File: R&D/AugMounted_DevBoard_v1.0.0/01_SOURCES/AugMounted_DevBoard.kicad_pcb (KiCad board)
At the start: 2 copper layers, 0 parts

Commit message: Schematic 90% done
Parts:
- added C1: C_0603_100nF_100V_X7R_10%, .mounted-lib:C_0603_1608Metric, F.Cu at (79.2, 96.4)
- added C10: C_0603_100nF_100V_X7R_10%, .mounted-lib:C_0603_1608Metric, F.Cu at (83.5, 96.4)
- added C11: C_0805_1uF_100V_X7S_20%, .mounted-lib:C_0805_1608Metric, F.Cu at (74.9, 108.8)
- added C12: C_0603_100nF_100V_X7R_10%, .mounted-lib:C_0603_1608Metric, F.Cu at (83.5, 99.1)
- added C13: C_0603_100nF_100V_X7R_10%, .mounted-lib:C_0603_1608Metric, F.Cu at (83.5, 101.7)
- added C14: C_0603_100nF_100V_X7R_10%, .mounted-lib:C_0603_1608Metric, F.Cu at (83.5, 104.4)
- added C15: C_0603_100nF_100V_X7R_10%, .mounted-lib:C_0603_1608Metric, F.Cu at (83.5, 107.0)
- added C16: C_0603_100nF_100V_X7R_10%, .mounted-lib:C_0603_1608Metric, F.Cu at (87.7, 96.4)
- added C17: C_0603_100nF_100V_X7R_10%, .mounted-lib:C_0603_1608Metric, F.Cu at (87.7, 99.1)
- added C18: C_0805_1uF_100V_X7S_20%, .mounted-lib:C_0805_1608Metric, F.Cu at (78.9, 57.0)
- added C19: C_0805_1uF_100V_X7S_20%, .mounted-lib:C_0805_1608Metric, F.Cu at (78.9, 60.0)
- added C2: C_0805_1uF_100V_X7S_20%, .mounted-lib:C_0805_1608Metric, F.Cu at (74.9, 96.6)
- added C20: C_0805_2.2uF_25V_X7R_20%, .mounted-lib:C_0805_1608Metric, F.Cu at (78.9, 63.1)
- added C21: C_0603_100nF_100V_X7R_10%, .mounted-lib:C_0603_1608Metric, F.Cu at (66.0, 56.8)
- added C22: C_0603_1.2nF_100V_X7R_5%, .mounted-lib:C_0603_1608Metric, F.Cu at (66.0, 59.4)
- added C23: C_1206_10uF_25V_X7R_10%, .mounted-lib:C_1206_3216Metric, F.Cu at (88.4, 57.1)
- added C24: C_1206_10uF_25V_X7R_10%, .mounted-lib:C_1206_3216Metric, F.Cu at (88.4, 60.5)
- added C25: C_1206_10uF_25V_X7R_10%, .mounted-lib:C_1206_3216Metric, F.Cu at (88.4, 63.8)
- added C26: C_1206_10uF_25V_X7R_10%, .mounted-lib:C_1206_3216Metric, F.Cu at (88.4, 67.2)
- added C27: C_0805_2.2uF_25V_X7R_20%, .mounted-lib:C_0805_1608Metric, F.Cu at (78.9, 66.1)
- added C28: C_0805_10uF_10V_X7R_10%, .mounted-lib:C_0805_1608Metric, F.Cu at (78.9, 69.2)
- added C29: C_0603_100nF_100V_X7R_10%, .mounted-lib:C_0603_1608Metric, F.Cu at (113.5, 116.7)
- added C3: C_0603_100nF_100V_X7R_10%, .mounted-lib:C_0603_1608Metric, F.Cu at (79.2, 99.1)
- added C30: C_0603_2.2uF_10V_X7R_10%, .mounted-lib:C_0603_1608Metric, F.Cu at (113.5, 119.4)
- added C31: C_0603_100nF_100V_X7R_10%, .mounted-lib:C_0603_1608Metric, F.Cu at (66.0, 62.1)
- added C32: C_0805_10uF_10V_X7R_10%, .mounted-lib:C_0805_1608Metric, F.Cu at (78.9, 72.2)
- added C33: C_0805_10uF_10V_X7R_10%, .mounted-lib:C_0805_1608Metric, F.Cu at (83.3, 57.0)
- added C36: C_0805_10uF_10V_X7R_10%, .mounted-lib:C_0805_1608Metric, F.Cu at (83.3, 60.0)
- added C37: C_0805_10uF_10V_X7R_10%, .mounted-lib:C_0805_1608Metric, F.Cu at (83.3, 63.1)
- added C38: C_0603_47nF_100V_X7R_10%, .mounted-lib:C_0603_1608Metric, F.Cu at (66.0, 64.7)
- added C39: C_0603_4.7uF_16V_X7R_10%, .mounted-lib:C_0603_1608Metric, F.Cu at (66.0, 67.4)
- added C4: C_0805_1uF_100V_X7S_20%, .mounted-lib:C_0805_1608Metric, F.Cu at (74.9, 99.7)
- added C40: C_0805_10uF_10V_X7R_10%, .mounted-lib:C_0805_1608Metric, F.Cu at (83.3, 66.1)
- added C41: C_0805_10uF_10V_X7R_10%, .mounted-lib:C_0805_1608Metric, F.Cu at (83.3, 69.2)
- added C42: C_0603_1uF_16V_X7R_10%, .mounted-lib:C_0603_1608Metric, F.Cu at (66.0, 70.0)
- added C43: C_0603_100nF_100V_X7R_10%, .mounted-lib:C_0603_1608Metric, F.Cu at (66.0, 72.7)
- added C5: C_0805_1uF_100V_X7S_20%, .mounted-lib:C_0805_1608Metric, F.Cu at (74.9, 102.7)
- added C6: C_0805_1uF_100V_X7S_20%, .mounted-lib:C_0805_1608Metric, F.Cu at (74.9, 105.8)
- added C7: C_0603_100nF_100V_X7R_10%, .mounted-lib:C_0603_1608Metric, F.Cu at (79.2, 101.7)
- added C8: C_0603_100nF_100V_X7R_10%, .mounted-lib:C_0603_1608Metric, F.Cu at (79.2, 104.4)
- added C9: C_0603_100nF_100V_X7R_10%, .mounted-lib:C_0603_1608Metric, F.Cu at (79.2, 107.0)
- added D1: D_V2FM10HM3/H, .mounted-lib:D_SMF_VISHAY, F.Cu at (109.2, 113.7)
- added D2: D_V2FM10HM3/H, .mounted-lib:D_SMF_VISHAY, F.Cu at (94.2, 63.5)
- added D3: D_SRV05-4, .mounted-lib:SOT-23-6_TECH_PUBLIC, F.Cu at (108.8, 117.6)
- added D4: D_1SS301, .mounted-lib:SOT-23_TOSHIBA, F.Cu at (88.5, 86.3)
- added D5: D_SRV05-4, .mounted-lib:SOT-23-6_TECH_PUBLIC, F.Cu at (93.8, 71.0)
- added J1: J_TYPE-C-31-M-13, .mounted-lib:J_TYPE-C-31-M-13, F.Cu at (99.0, 120.6)
- added J2: J_FH43BW-61S-0.2SHW, .mounted-lib:J_FH43BW-61S-0.2SHW, F.Cu at (80.4, 92.8)
- added J3: J_JST_S2B-PH-SM4-TB, .mounted-lib:J_JST_S2B-PH-SM4-TB, F.Cu at (81.5, 79.4)
- added JP1: SolderJumper_2_Bridged, Jumper:SolderJumper-2_P1.3mm_Bridged_RoundedPad1.0x1.5mm, F.Cu at (79.3, 110.1)
- added JP2: SolderJumper_2_Bridged, Jumper:SolderJumper-2_P1.3mm_Bridged_RoundedPad1.0x1.5mm, F.Cu at (79.3, 113.7)
- added JP3: SolderJumper_2_Bridged, Jumper:SolderJumper-2_P1.3mm_Bridged_RoundedPad1.0x1.5mm, F.Cu at (79.3, 117.2)
- added L1: L_7447789003, .mounted-lib:L_7447789003, F.Cu at (68.4, 81.5)
- added L3: L_TFM252012ALMA1R0MTAA, .mounted-lib:TFM252012ALMA1R0MTAA, F.Cu at (79.1, 86.4)
- added L4: L_FNR3015S2R2MT, .mounted-lib:L_FNR3015S2R2MT, F.Cu at (111.8, 87.8)
- added Q1: Q_BSS123WQ-7-F, .mounted-lib:SOT-323_SC-70_DIODES_INC, F.Cu at (86.3, 110.3)
- added Q2: Q_BSS123WQ-7-F, .mounted-lib:SOT-323_SC-70_DIODES_INC, F.Cu at (94.0, 75.7)
- added Q3: Q_HSS2P10, .mounted-lib:SOT-23-3_HUASHUO, F.Cu at (87.8, 71.1)
- added Q5: Q_BSS123WQ-7-F, .mounted-lib:SOT-323_SC-70_DIODES_INC, F.Cu at (94.0, 79.5)
- added R1: R_0603_100k_1%_0.1W, .mounted-lib:R_0603_1608Metric, F.Cu at (87.7, 101.7)
- added R10: R_0603_100k_1%_0.1W, .mounted-lib:R_0603_1608Metric, F.Cu at (70.3, 70.0)
- added R11: R_0603_0R_1%_0.1W, .mounted-lib:R_0603_1608Metric, F.Cu at (70.3, 72.7)
- added R13: R_0603_1M_1%_0.1W, .mounted-lib:R_0603_1608Metric, F.Cu at (70.3, 75.3)
- added R14: R_0603_10k_1%_0.1W, .mounted-lib:R_0603_1608Metric, F.Cu at (74.5, 56.8)
- added R15: R_0603_31.2k_0.5%_0.1W, .mounted-lib:R_0603_1608Metric, F.Cu at (74.5, 59.4)
- added R16: R_0603_5.23k_1%_0.1W, .mounted-lib:R_0603_1608Metric, F.Cu at (74.5, 62.1)
- added R17: R_0603_10k_1%_0.1W, .mounted-lib:R_0603_1608Metric, F.Cu at (74.5, 64.7)
- added R18: R_0603_10k_1%_0.1W, .mounted-lib:R_0603_1608Metric, F.Cu at (74.5, 67.4)
- added R19: R_0603_316R_0.5%_0.1W, .mounted-lib:R_0603_1608Metric, F.Cu at (74.5, 70.0)
- added R2: R_0603_100k_1%_0.1W, .mounted-lib:R_0603_1608Metric, F.Cu at (87.7, 104.4)
- added R21: R_0603_100k_1%_0.1W, .mounted-lib:R_0603_1608Metric, F.Cu at (74.5, 72.7)
- added R3: R_0603_100k_1%_0.1W, .mounted-lib:R_0603_1608Metric, F.Cu at (66.0, 75.3)
- added R4: R_0603_42.2k_1%_0.1W, .mounted-lib:R_0603_1608Metric, F.Cu at (70.3, 56.8)
- added R5: R_0603_200k_1%_0.1W, .mounted-lib:R_0603_1608Metric, F.Cu at (70.3, 59.4)
- added R6: R_0603_26.7k_1%_0.1W, .mounted-lib:R_0603_1608Metric, F.Cu at (70.3, 62.1)
- added R7: R_0603_100k_1%_0.1W, .mounted-lib:R_0603_1608Metric, F.Cu at (70.3, 64.7)
- added R9: R_0603_100k_1%_0.1W, .mounted-lib:R_0603_1608Metric, F.Cu at (70.3, 67.4)
- added RT1: RT_TX06F103F3435ER, .mounted-lib:NTCG16_XXX_TDK, F.Cu at (93.8, 87.1)
- added SJ1: SOLDER_JUMPER_3PIN_NC, .mounted-lib:SOLDER_JUMPER_3PIN_NC, F.Cu at (94.0, 67.0)
- added TP1: TESTPOINT_1MM, .mounted-lib:TESTPOINT_1MM, F.Cu at (82.8, 109.7)
- added TP2: TESTPOINT_1MM, .mounted-lib:TESTPOINT_1MM, F.Cu at (82.8, 112.3)
- added TP3: TESTPOINT_1MM, .mounted-lib:TESTPOINT_1MM, F.Cu at (82.8, 115.0)
- added TP4: TESTPOINT_1.5MM, .mounted-lib:TESTPOINT_1.5MM, F.Cu at (74.5, 78.2)
- added U1: ESP32-S3-WROOM-1U-N16R8, .mounted-lib:ESP32-S3-WROOM-1U, F.Cu at (102.2, 100.8)
- added U10: U_TPS63001DRCR, .mounted-lib:PVSON-N10_TEXAS_INSTRUMENTS, F.Cu at (89.1, 81.8)
- added U2: U_BQ24296MRGER, .mounted-lib:VQFN-24_TEXAS_INSTRUMENTS, F.Cu at (94.3, 58.6)
- added U3: U_MAX17048G+T10, .mounted-lib:TDFN-8_MAXIM_INTEGRATED, F.Cu at (83.8, 86.3)
- added U4: U_TXB0108PWR, .mounted-lib:TSSOP-20_4.4x6.5mm_P0.65mm_TEXAS_INSTRUMENTS, F.Cu at (68.3, 94.4)
- added U5: U_TXB0108PWR, .mounted-lib:TSSOP-20_4.4x6.5mm_P0.65mm_TEXAS_INSTRUMENTS, F.Cu at (68.3, 102.4)
- added U6: U_TXB0108PWR, .mounted-lib:TSSOP-20_4.4x6.5mm_P0.65mm_TEXAS_INSTRUMENTS, F.Cu at (68.3, 110.5)
- added U7: U_TPS61087DRCR, .mounted-lib:PVSON-N10_TEXAS_INSTRUMENTS, F.Cu at (89.1, 76.4)
- added U8: U_LP3987H-18B5F, .mounted-lib:SOT-23-5_LOW_POWER, F.Cu at (94.3, 83.7)
- added U9: U_VCNL4040M3OE, .mounted-lib:VCNL4040_4X2X1.1_VISHAY, F.Cu at (114.6, 93.4)
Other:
- board outline added: 9.5 x 6.5 mm

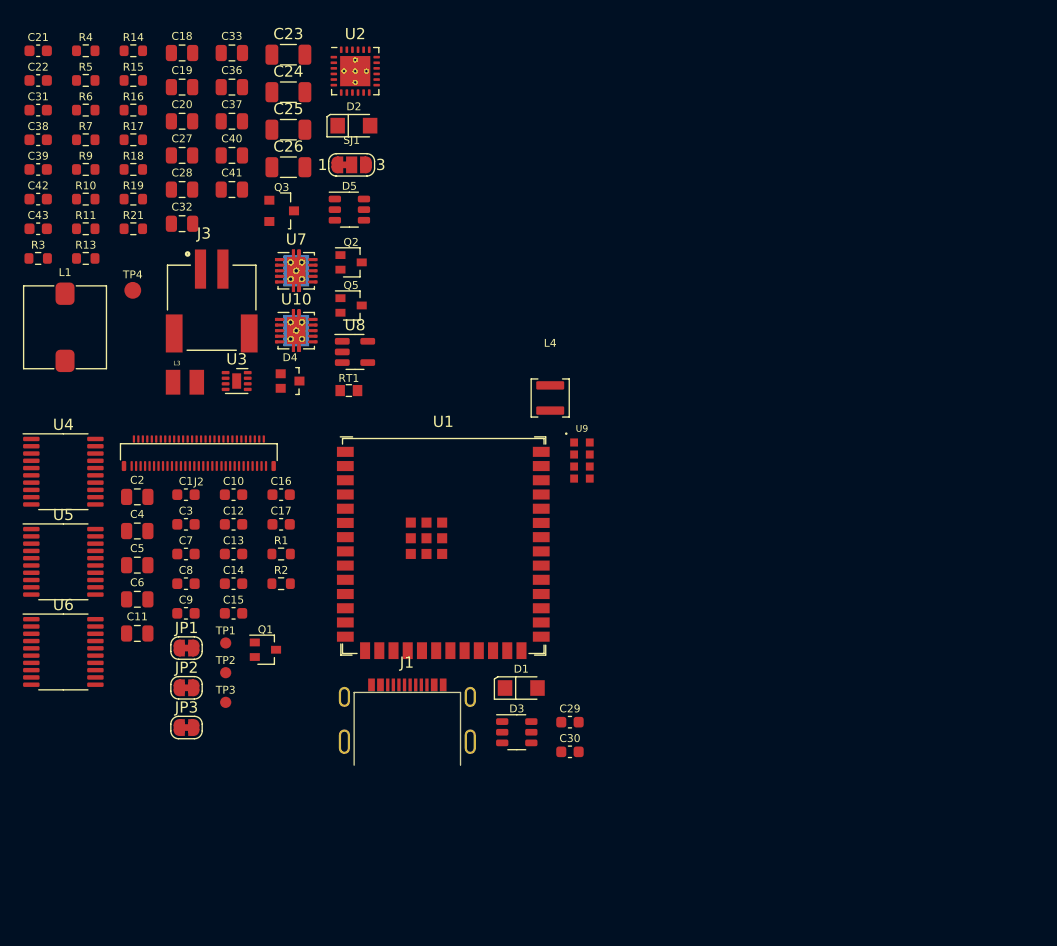
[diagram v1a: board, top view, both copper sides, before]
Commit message: Schematic done
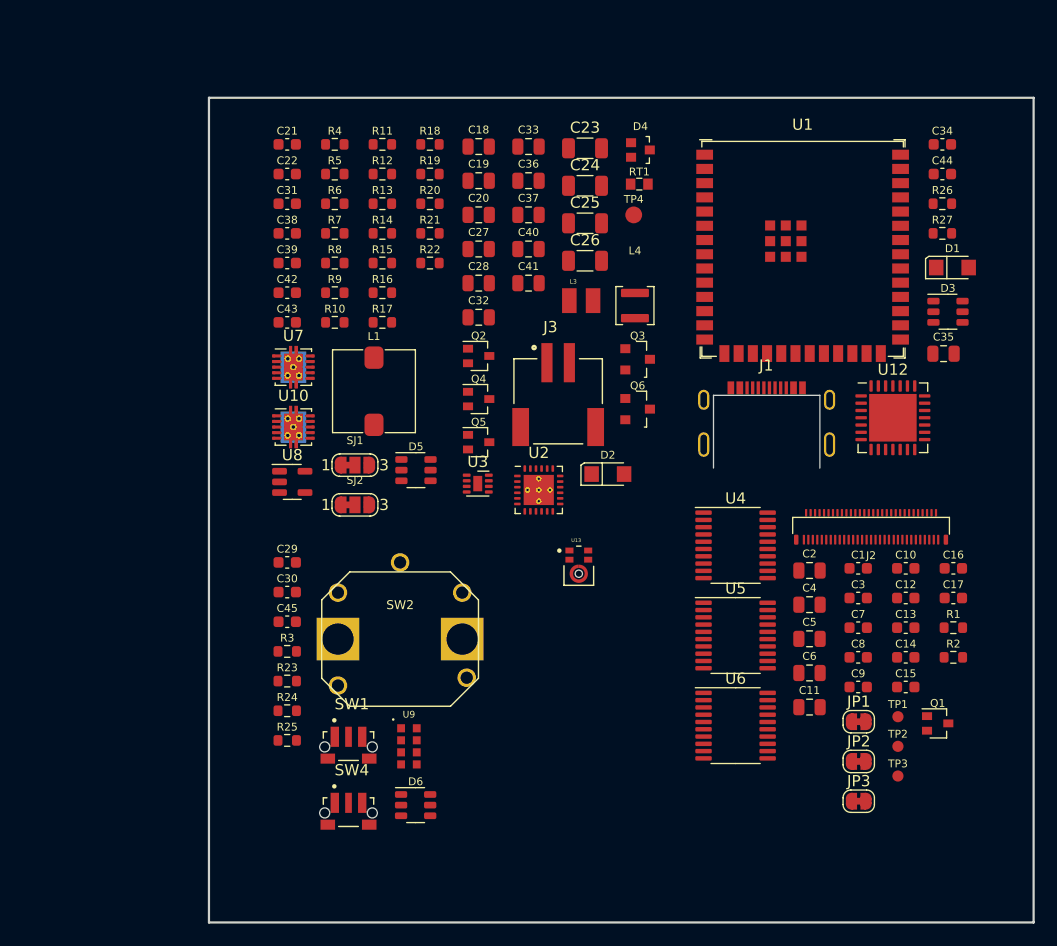
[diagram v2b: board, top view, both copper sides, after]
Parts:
- added C34: C_0603_100nF_100V_X7R_10%, .mounted-lib:C_0603_1608Metric, F.Cu at (146.8, 65.1)
- added C35: C_0805_22uF_10V_XR7_20%, .mounted-lib:C_0805_1608Metric, F.Cu at (146.9, 83.8)
- added C44: C_0603_100nF_100V_X7R_10%, .mounted-lib:C_0603_1608Metric, F.Cu at (146.8, 67.8)
- added C45: C_0603_100nF_100V_X7R_10%, .mounted-lib:C_0603_1608Metric, F.Cu at (88.3, 107.8)
- added D6: D_SRV05-4, .mounted-lib:SOT-23-6_TECH_PUBLIC, F.Cu at (99.7, 124.1)
- added Q4: Q_BSS123WQ-7-F, .mounted-lib:SOT-323_SC-70_DIODES_INC, F.Cu at (105.4, 87.9)
- added Q6: Q_HSS2P10, .mounted-lib:SOT-23-3_HUASHUO, F.Cu at (119.6, 88.8)
- added R12: R_0603_0R_1%_0.1W, .mounted-lib:R_0603_1608Metric, F.Cu at (96.8, 67.8)
- added R20: R_0603_100k_1%_0.1W, .mounted-lib:R_0603_1608Metric, F.Cu at (101.0, 70.4)
- added R22: R_0603_0R_1%_0.1W, .mounted-lib:R_0603_1608Metric, F.Cu at (101.0, 75.7)
- added R23: R_0603_10k_1%_0.1W, .mounted-lib:R_0603_1608Metric, F.Cu at (88.3, 113.1)
- added R24: R_0603_100k_1%_0.1W, .mounted-lib:R_0603_1608Metric, F.Cu at (88.3, 115.7)
- added R25: R_0603_100k_1%_0.1W, .mounted-lib:R_0603_1608Metric, F.Cu at (88.3, 118.4)
- added R26: R_0603_4.7k_1%_0.1W, .mounted-lib:R_0603_1608Metric, F.Cu at (146.8, 70.4)
- added R27: R_0603_4.7k_1%_0.1W, .mounted-lib:R_0603_1608Metric, F.Cu at (146.8, 73.1)
- added R8: R_0603_1M_1%_0.1W, .mounted-lib:R_0603_1608Metric, F.Cu at (92.5, 75.7)
- added SJ2: SOLDER_JUMPER_3PIN_NC, .mounted-lib:SOLDER_JUMPER_3PIN_NC, F.Cu at (94.3, 97.3)
- added SW1: SW_SKRTLAE010, .mounted-lib:SW_SKRTLAE010, F.Cu at (93.7, 118.9)
- added SW2: SW_EC12D1564404, .mounted-lib:SW_EC12D1564404, F.Cu at (98.4, 109.3)
- added SW4: SW_SKRTLAE010, .mounted-lib:SW_SKRTLAE010, F.Cu at (93.7, 124.8)
- added U12: U_MCP23017T-E/ML, .mounted-lib:QFN-28-1EP_6x6mm_P0.65mm_EP4.25x4.25mm_MICROCHIP, F.Cu at (142.4, 89.5)
- added U13: ICS‐41350, .mounted-lib:U_ICS-41350, F.Cu at (114.3, 102.8)
- C29: value C_0603_100nF_100V_X7R_10% -> C_0603_2.2uF_10V_X7R_10%
- C30: value C_0603_2.2uF_10V_X7R_10% -> C_0603_100nF_100V_X7R_10%
- R11: value R_0603_0R_1%_0.1W -> R_0603_1M_1%_0.1W
- R3: value R_0603_100k_1%_0.1W -> R_0603_10k_1%_0.1W
- moved C1 60.4 mm to (139.3, 103.0)
- moved C10 60.4 mm to (143.5, 103.0)
- moved C12 60.4 mm to (143.5, 105.6)
- moved C13 60.4 mm to (143.5, 108.3)
- moved C14 60.4 mm to (143.5, 110.9)
- moved C15 60.4 mm to (143.5, 113.6)
- moved C16 60.4 mm to (147.8, 103.0)
- moved C17 60.4 mm to (147.8, 105.6)
- moved C3 60.4 mm to (139.3, 105.6)
- moved C7 60.4 mm to (139.3, 108.3)
- moved C8 60.4 mm to (139.3, 110.9)
- moved C9 60.4 mm to (139.3, 113.6)
- moved R1 60.4 mm to (147.8, 108.3)
- moved R2 60.4 mm to (147.8, 110.9)
- moved Q1 60.4 mm to (146.4, 116.8)
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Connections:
- net /Battery Management/BUTTON_PIN renamed /Battery Management/ENCODER_BUTTON
- net /OLED/VDD1 renamed /1.8V_LCD
- net Net-(D4-A1) renamed /ENCODER_S2
- net Net-(U2-STAT) renamed /Battery Management/CHARGE_STATUS
- net Net-(U2-~{PG}) renamed /Battery Management/PGOOD
- C42 pad 1: Net-(C42-Pad1) -> VBUS
- D1 pad 1: unconnected-(D1-K-Pad1) -> VBUS
- D1 pad 2: unconnected-(D1-A-Pad2) -> /MCU/VBUS_USB
- D3 pad 1: unconnected-(D3-IO1-Pad1) -> /MCU/USB_D+
- D3 pad 2: unconnected-(D3-VN-Pad2) -> GND
- D3 pad 3: unconnected-(D3-IO2-Pad3) -> /MCU/CC1
- D3 pad 4: unconnected-(D3-IO3-Pad4) -> /MCU/USB_D-
- D3 pad 5: unconnected-(D3-VP-Pad5) -> /MCU/VBUS_USB
- D3 pad 6: unconnected-(D3-IO4-Pad6) -> /MCU/CC2
- J1 pad A1: Net-(J1-GND-PadA1) -> GND
- J1 pad A12: Net-(J1-GND-PadA1) -> GND
- J1 pad A4: Net-(J1-VBUS-PadA4) -> /MCU/VBUS_USB
- J1 pad A6: unconnected-(J1-DP1-PadA6) -> /MCU/USB_D+
- J1 pad A7: unconnected-(J1-DN1-PadA7) -> /MCU/USB_D-
- J1 pad A9: Net-(J1-VBUS-PadA4) -> /MCU/VBUS_USB
- J1 pad B1: Net-(J1-GND-PadA1) -> GND
- J1 pad B12: Net-(J1-GND-PadA1) -> GND
- J1 pad B4: Net-(J1-VBUS-PadA4) -> /MCU/VBUS_USB
- J1 pad B6: unconnected-(J1-DP2-PadB6) -> /MCU/USB_D+
- J1 pad B7: unconnected-(J1-DN2-PadB7) -> /MCU/USB_D-
- J1 pad B9: Net-(J1-VBUS-PadA4) -> /MCU/VBUS_USB
- J1 pad GND: Net-(J1-GND-PadA1) -> GND
- J2 pad 26: /OLED/G2_1.8V -> /OLED/RGB_LSB_1.8V
- R11 pad 1: Net-(Q3-G) -> /Battery Management/1.8V_ENABLE
- R11 pad 2: Net-(Q2-D) -> GND
- R3 pad 1: /Battery Management/1.8V_ENABLE -> +3.3V
- R3 pad 2: GND -> /ENCODER_B
- R9 pad 2: Net-(R9-Pad2) -> /ENCODER_S1
- U1 pad 1: Net-(U1-GND-Pad1) -> GND
- U1 pad 10: unconnected-(U1-GPIO17/U1TXD/ADC2_CH6-Pad10) -> /ENCODER_B
- U1 pad 11: unconnected-(U1-GPIO18/U1RXD/ADC2_CH7/CLK_OUT3-Pad11) -> /ENCODER_A
- U1 pad 12: unconnected-(U1-GPIO8/TOUCH8/ADC1_CH7/SUBSPICS1-Pad12) -> /XCLR
- U1 pad 13: unconnected-(U1-GPIO19/U1RTS/ADC2_CH8/CLK_OUT2/USB_D--Pad13) -> /MCU/USB_D-
- U1 pad 14: unconnected-(U1-GPIO20/U1CTS/ADC2_CH9/CLK_OUT1/USB_D+-Pad14) -> /MCU/USB_D+
- U1 pad 15: unconnected-(U1-GPIO3/TOUCH3/ADC1_CH2-Pad15) -> /XHD
- U1 pad 16: unconnected-(U1-GPIO46-Pad16) -> /HVD
- U1 pad 17: unconnected-(U1-GPIO9/TOUCH9/ADC1_CH8/FSPIHD/SUBSPIHD-Pad17) -> /MCLK
- U1 pad 18: unconnected-(U1-GPIO10/TOUCH10/ADC1_CH9/FSPICS0/FSPIIO4/SUBSPICS0-Pad18) -> /B5
- U1 pad 19: unconnected-(U1-GPIO11/TOUCH11/ADC2_CH0/FSPID/FSPIIO5/SUBSPID-Pad19) -> /B4
- U1 pad 2: unconnected-(U1-3V3-Pad2) -> +3.3V
- U1 pad 20: unconnected-(U1-GPIO12/TOUCH12/ADC2_CH1/FSPICLK/FSPIIO6/SUBSPICLK-Pad20) -> /B3
- U1 pad 21: unconnected-(U1-GPIO13/TOUCH13/ADC2_CH2/FSPIQ/FSPIIO7/SUBSPIQ-Pad21) -> /B2
- U1 pad 22: unconnected-(U1-GPIO14/TOUCH14/ADC2_CH3/FSPIWP/FSPIDQS/SUBSPIWP-Pad22) -> /B1
- U1 pad 23: unconnected-(U1-GPIO21-Pad23) -> /I2S_PDM_DATA
- U1 pad 24: unconnected-(U1-GPIO47/SPICLK_P/SUBSPICLK_P_DIFF-Pad24) -> /G5
- U1 pad 25: unconnected-(U1-GPIO48/SPICLK_N/SUBSPICLK_N_DIFF-Pad25) -> /G4
- U1 pad 26: unconnected-(U1-GPIO45-Pad26) -> /G3
- U1 pad 31: unconnected-(U1-GPIO38/FSPIWP/SUBSPIWP-Pad31) -> /G2
- U1 pad 32: unconnected-(U1-MTCK/GPIO39/CLK_OUT3/SUBSPICS1-Pad32) -> /G1
- U1 pad 33: unconnected-(U1-MTDO/GPIO40/CLK_OUT2-Pad33) -> /R5
- U1 pad 34: unconnected-(U1-MTDI/GPIO41/CLK_OUT1-Pad34) -> /R4
- U1 pad 35: unconnected-(U1-MTMS/GPIO42-Pad35) -> /R3
- U1 pad 36: unconnected-(U1-U0RXD/GPIO44/CLK_OUT2-Pad36) -> /Battery Management/ESP_POWER_EN
- U1 pad 37: unconnected-(U1-U0TXD/GPIO43/CLK_OUT1-Pad37) -> /R2
- U1 pad 38: unconnected-(U1-GPIO2/TOUCH2/ADC1_CH1-Pad38) -> /SCL
- U1 pad 39: unconnected-(U1-GPIO1/TOUCH1/ADC1_CH0-Pad39) -> /R1
- U1 pad 4: unconnected-(U1-GPIO4/TOUCH4/ADC1_CH3-Pad4) -> /MISO
- U1 pad 40: Net-(U1-GND-Pad1) -> GND
- U1 pad 41: Net-(U1-GND-Pad1) -> GND
- U1 pad 5: unconnected-(U1-GPIO5/TOUCH5/ADC1_CH4-Pad5) -> /MOSI
- U1 pad 6: unconnected-(U1-GPIO6/TOUCH6/ADC1_CH5-Pad6) -> /SCK
- U1 pad 7: unconnected-(U1-GPIO7/TOUCH7/ADC1_CH6-Pad7) -> /CS
- U1 pad 8: unconnected-(U1-GPIO15/U0RTS/ADC2_CH4/XTAL_32K_P-Pad8) -> /SDA
- U1 pad 9: unconnected-(U1-GPIO16/U0CTS/ADC2_CH5/XTAL_32K_N-Pad9) -> /I2S_PDM_CLK
- U2 pad 1: Net-(C42-Pad1) -> VBUS
- U2 pad 2: GND -> Net-(SJ2-C)
- U2 pad 24: Net-(C42-Pad1) -> VBUS
- U2 pad 25: unconnected-(U2-PAD-Pad25) -> GND
- U2 pad 5: /Battery Management/SCL -> /SCL
- U2 pad 6: /Battery Management/SDA -> /SDA
- U3 pad 7: /Battery Management/SCL -> /SCL
- U3 pad 8: /Battery Management/SDA -> /SDA
- U4 pad 12: /OLED/G3 -> /G2
- U4 pad 13: /OLED/G2 -> /G1
- U4 pad 14: /OLED/G1 -> unconnected-(U4-B6-Pad14)
- U4 pad 15: /OLED/R5 -> /R5
- U4 pad 16: /OLED/R4 -> /R4
- U4 pad 17: /OLED/R3 -> /R3
- U4 pad 18: /OLED/R2 -> /R2
- U4 pad 20: /OLED/R1 -> /R1
- U4 pad 7: /OLED/G2_1.8V -> unconnected-(U4-A6-Pad7)
- U5 pad 12: /OLED/B5 -> /B5
- U5 pad 13: /OLED/B4 -> /B4
- U5 pad 14: /OLED/B3 -> /B3
- U5 pad 15: /OLED/B2 -> /B2
- U5 pad 16: /OLED/B1 -> /B1
- U5 pad 17: /OLED/G6 -> /G5
- U5 pad 18: /OLED/G5 -> /G4
- U5 pad 20: /OLED/G4 -> /G3
- U6 pad 12: /OLED/CS -> /CS
- U6 pad 13: /OLED/SCK -> /SCK
- U6 pad 14: /OLED/MOSI -> /MOSI
- U6 pad 15: /OLED/MISO -> /MISO
- U6 pad 16: /OLED/XCLR -> /XCLR
- U6 pad 17: /OLED/HVD -> /HVD
- U6 pad 18: /OLED/XHD -> /XHD
- U6 pad 20: /OLED/MCLK -> /MCLK
- U8 pad 3: /Battery Management/1.8V_ENABLE -> +3.3V
- U9 pad 7: unconnected-(U9-SDA-Pad7) -> /SDA
- U9 pad 8: unconnected-(U9-SCL-Pad8) -> /SCL
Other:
- board size 9.5 x 6.5 mm -> 73.7 x 73.7 mm

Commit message: First revision of the layout
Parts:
- added C503: C_0603_100nF_100V_X7R_10%, .mounted-lib:C_0603_1608Metric, F.Cu at (102.9, 128.4)
- added LOGO1: mounted_logo, .mounted-lib:mounted_logo, F.Cu at (82.7, 69.4)
- added U503: LIS2DW12, Package_LGA:LGA-12_2x2mm_P0.5mm, F.Cu at (103.2, 126.3)
- JP401: renamed from JP1; moved to B.Cu
- JP402: renamed from JP2; moved to B.Cu
- JP403: renamed from JP3; moved to B.Cu
- TP301: renamed from TP4; moved to B.Cu
- TP401: renamed from TP1; moved to B.Cu
- TP402: renamed from TP2; moved to B.Cu
- TP403: renamed from TP3; moved to B.Cu
- moved R306 80.9 mm to (103.0, 151.3)
- moved R305 80.5 mm to (103.0, 145.3)
- moved C304 80.2 mm to (99.4, 154.5), turned to 180 degrees
- moved C202 80.2 mm to (101.1, 131.0), turned to -90 degrees
- moved C301 76.9 mm to (99.4, 148.1), turned to 180 degrees
- moved J401 75.6 mm to (88.0, 153.8)
- moved R503 75.2 mm to (148.1, 161.3), turned to -90 degrees
- moved R401 75.0 mm to (81.8, 146.7), turned to -90 degrees
- moved C413 74.2 mm to (81.8, 149.8), turned to 90 degrees
- moved R307 74.0 mm to (103.0, 149.7), turned to 180 degrees
- moved R402 72.0 mm to (86.8, 146.7), turned to -90 degrees
- moved SW502 72.0 mm to (151.8, 161.5), turned to 180 degrees
- moved Q401 68.9 mm to (84.3, 146.7)
- moved C404 68.3 mm to (83.5, 143.5)
- moved R504 67.7 mm to (133.9, 168.4), turned to 180 degrees
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- renumbered C35 to C201, C34 to C202, C44 to C203, C20 to C301, C42 to C302, C41 to C303, C27 to C304, C43 to C305, C28 to C306, C31 to C307, C38 to C308, C40 to C309, C39 to C310, C32 to C311, C36 to C312, C33 to C313, C37 to C314, C18 to C315, C19 to C316, C21 to C317, C22 to C318, C23 to C319, C24 to C320, C25 to C321, C26 to C322, C15 to C401, C17 to C402, C16 to C403, C14 to C404, C12 to C405, C13 to C406, C3 to C407, C9 to C408, C8 to C409, C7 to C410, C11 to C411, C2 to C412, C1 to C413, C10 to C414, C4 to C415, C5 to C416, C6 to C417, C29 to C501, C45 to C502, C30 to C504, D3 to D201, D1 to D202, D5 to D301, D4 to D302, D2 to D303, D6 to D501, J1 to J201, J3 to J301, J2 to J401, L4 to L301, L3 to L302, L1 to L303, Q4 to Q301, Q6 to Q302, Q5 to Q303, Q2 to Q304, Q3 to Q305, Q1 to Q401, R26 to R201, R27 to R202, R19 to R301, R14 to R302, R17 to R303, R18 to R304, R11 to R305, R20 to R306, R22 to R307, R16 to R308, R15 to R309, R21 to R310, R7 to R311, R9 to R312, R13 to R313, R10 to R314, R12 to R315, R4 to R316, R5 to R317, R6 to R318, R8 to R319, R2 to R401, R1 to R402, R23 to R501, R3 to R502, R24 to R503, R25 to R504, RT1 to RT301, SJ1 to SJ301, SJ2 to SJ302, SW2 to SW501, SW1 to SW502, SW4 to SW503, U1 to U201, U12 to U202, U8 to U301, U3 to U302, U2 to U303, U10 to U304, U7 to U305, U4 to U401, U5 to U402, U6 to U403, U9 to U501, U13 to U502
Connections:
- D201 pad 3: /MCU/CC1 -> /MCU/USB_D-
- D201 pad 4: /MCU/USB_D- -> /MCU/CC1
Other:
- board size 73.7 x 73.7 mm -> 25.1 x 93.7 mm
- board text added: "BATTERY 1S 1000mAh"
- board text added: "PLACE UNDER BATTERY"

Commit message: Changed layout to a banana shape
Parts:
- removed the R503 at (148.1, 161.3)
- removed SW502, SW503: SW_SKRTLAE010, .mounted-lib:SW_SKRTLAE010
- added C201: C_0603_1uF_16V_X7R_10%, .mounted-lib:C_0603_1608Metric, F.Cu at (370.9, 85.9)
- added D502: D_SRV05-4, .mounted-lib:SOT-23-6_TECH_PUBLIC, F.Cu at (347.5, 57.6)
- added F301: F_MFU0603FF05000P100, .mounted-lib:R_0603_1608Metric, F.Cu at (342.4, 38.3)
- added J501: J_0788641001_PAD, .mounted-lib:J_788641001_PAD, B.Cu at (347.5, 57.7)
- added J502: J_0788641001, .mounted-lib:J_788641001, F.Cu at (219.6, -43.7)
- added J503: J_0788641001, .mounted-lib:J_788641001, F.Cu at (219.6, -37.3)
- added J504: J_0788641001_PAD, .mounted-lib:J_788641001_PAD, B.Cu at (337.6, 20.4)
- added LED201: LED_MHPC3528CRGBCT, .mounted-lib:LED_MHPC3528CRGBCT, F.Cu at (354.7, 15.3)
- added LED501: LED_LTW-010DCG, .mounted-lib:LED_LTW-010DCG, F.Cu at (366.6, 89.5)
- added LED502: LED_LTW-010DCG, .mounted-lib:LED_LTW-010DCG, F.Cu at (370.2, 92.5)
- added LED503: LED_LTW-010DCG, .mounted-lib:LED_LTW-010DCG, F.Cu at (373.8, 95.5)
- added Q501: Q_BSS123WQ-7-F, .mounted-lib:SOT-323_SC-70_DIODES_INC, F.Cu at (373.1, 91.4)
- added R201: R_0603_10k_1%_0.1W, .mounted-lib:R_0603_1608Metric, F.Cu at (371.3, 88.2)
- added R202: R_0603_33R_1%_0.1W, .mounted-lib:R_0603_1608Metric, F.Cu at (357.2, 17.6)
- added R203: R_0603_56R_1%_0.1W, .mounted-lib:R_0603_1608Metric, F.Cu at (357.2, 14.4)
- added R204: R_0603_56R_1%_0.1W, .mounted-lib:R_0603_1608Metric, F.Cu at (354.8, 18.6)
- added R501: R_0603_0R_1%_0.1W, .mounted-lib:R_0603_1608Metric, F.Cu at (348.9, 60.1)
- added R505: R_0603_100k_1%_0.1W, .mounted-lib:R_0603_1608Metric, F.Cu at (358.1, 69.9)
- added R506: R_0603_100k_1%_0.1W, .mounted-lib:R_0603_1608Metric, F.Cu at (370.4, 89.5)
- added R507: R_0603_0R_1%_0.1W, .mounted-lib:R_0603_1608Metric, F.Cu at (375.8, 93.4)
- added SW601: SW_EC12D1564404, .mounted-lib:SW_EC12D1564404, F.Cu at (234.4, -38.8)
- added SW602: SW_SKRTLAE010, .mounted-lib:SW_SKRTLAE010, F.Cu at (245.7, -43.9)
- added SW603: SW_SKRTLAE010, .mounted-lib:SW_SKRTLAE010, F.Cu at (245.7, -38.0)
- added TP201: TESTPOINT_1.5MM, .mounted-lib:TESTPOINT_1.5MM, F.Cu at (212.5, 32.8)
- added TP202: TESTPOINT_1.5MM, .mounted-lib:TESTPOINT_1.5MM, F.Cu at (212.5, 29.7)
- LOGO101: renamed from LOGO1; moved to B.Cu
- SW501: value SW_EC12D1564404 -> SW_SKRTLAE010; footprint .mounted-lib:SW_EC12D1564404 -> .mounted-lib:SW_SKRTLAE010
- U201: moved to B.Cu
- moved R401 302.7 mm to (375.4, 73.0), turned to -35 degrees
- moved LOGO101 302.7 mm to (385.3, 75.6), turned to 145 degrees
- moved TP401 302.4 mm to (387.3, 81.0), turned to -35 degrees
- moved Q401 302.3 mm to (377.0, 71.1), turned to 55 degrees
- moved R402 301.7 mm to (379.4, 73.2), turned to 145 degrees
- moved C413 300.9 mm to (375.5, 84.7), turned to 145 degrees
- moved TP402 300.8 mm to (386.3, 82.4), turned to -35 degrees
- moved C408 300.5 mm to (376.4, 83.4), turned to 145 degrees
- moved J401 299.8 mm to (380.0, 85.7), turned to 55 degrees
- moved TP403 299.2 mm to (385.4, 83.7), turned to -35 degrees
- moved C404 298.7 mm to (373.3, 70.9), turned to 55 degrees
- moved JP403 298.5 mm to (380.6, 89.0), turned to -35 degrees
- moved JP402 297.9 mm to (382.1, 87.0), turned to -35 degrees
- moved C409 297.6 mm to (377.4, 82.1), turned to 145 degrees
- moved C411 297.5 mm to (384.5, 78.4), turned to -35 degrees
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- renumbered C201 to C202, C202 to C203, C203 to C204, R201 to R205, R202 to R206, R501 to R503
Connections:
- D501 pad 4: /ENCODER_S1 -> /ENCODER_S2
- D501 pad 6: /ENCODER_S2 -> /ENCODER_S1
- J301 pad 2: /Battery Management/VBAT -> Net-(J301-+)
- R504 pad 1: GND -> +3.3V
- R504 pad 2: /User Input/BUTTON2 -> /BUTTON1
- U201 pad 27: unconnected-(U201-GPIO0/BOOT-Pad27) -> Net-(U201-GPIO0/BOOT)
- U201 pad 3: unconnected-(U201-EN-Pad3) -> Net-(U201-EN)
- U202 pad 1: /Battery Management/PGOOD -> /MCU/RGB_LED_R
- U202 pad 2: unconnected-(U202-GPB5-Pad2) -> /MCU/RGB_LED_G
- U202 pad 20: unconnected-(U202-GPA3-Pad20) -> /Battery Management/CHARGE_STATUS
- U202 pad 21: unconnected-(U202-GPA4-Pad21) -> /Battery Management/PGOOD
- U202 pad 26: /MCU/BUTTON1 -> /BUTTON1
- U202 pad 27: /MCU/BUTTON2 -> /BUTTON2
- U202 pad 28: /Battery Management/CHARGE_STATUS -> /LEDS_ENABLE
- U202 pad 3: unconnected-(U202-GPB6-Pad3) -> /MCU/RGB_LED_B
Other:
- board size 25.1 x 93.7 mm -> 56.8 x 89.5 mm
